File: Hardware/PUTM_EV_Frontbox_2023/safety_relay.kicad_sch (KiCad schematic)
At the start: 2 parts, among them Q1 2N7002

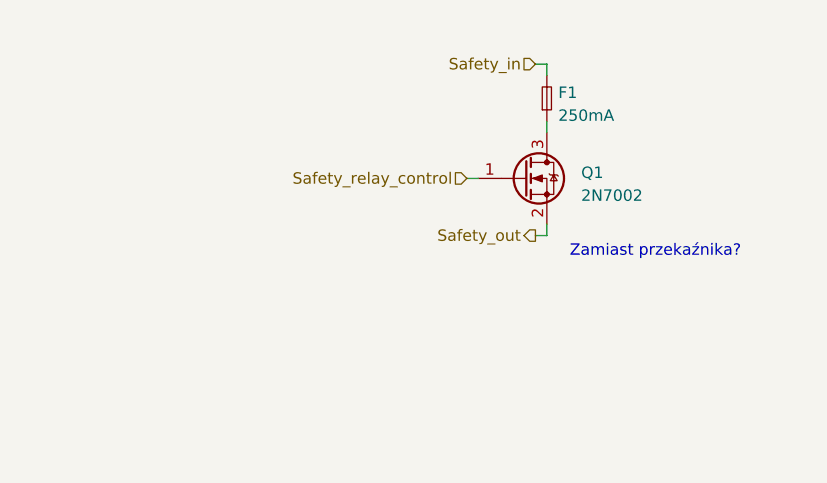
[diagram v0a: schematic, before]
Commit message: Added power section, replaced SWPS
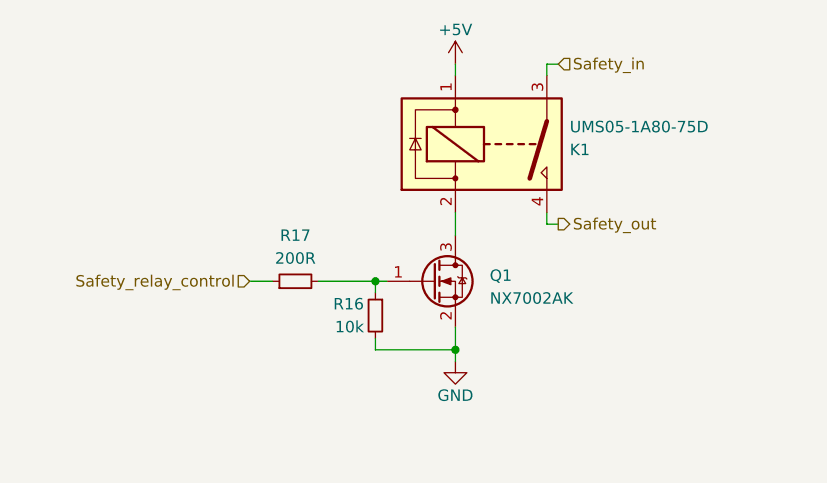
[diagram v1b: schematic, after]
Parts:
- removed F1: 250mA, symbol Device:Fuse_Small
- added K1: UMS05-1A80-75D, Relay_THT:Relay_StandexMeder_UMS, symbol Relay:UMS05-1A80-75D
- added R16: 10k, symbol Device:R_Small
- added R17: 200R, symbol Device:R_Small
- Q1: value 2N7002 -> NX7002AK
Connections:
- net Safety_in: now also K1.3
- net Safety_out: now also K1.4; no longer Q1.2 (S)
- net Safety_relay_control: now also R17.1; no longer Q1.1 (G)
- net at Q1.3 (D): now also K1.2
- new net: Q1.1 (G), R16.1, R17.2
- new net +5V: K1.1
- new net GND: Q1.2 (S), R16.2
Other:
- note removed: "Zamiast przekaźnika?"
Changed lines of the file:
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@@
     (comment 1 "Reviewer:")
   )
-  (wire (pts (xy 147.32 85.09) (xy 147.32 83.82))
-    (stroke (width 0) (type default))
-  )
-  (wire (pts (xy 138.43 78.74) (xy 139.7 78.74))
-    (stroke (width 0) (type default))
-  )
-  (wire (pts (xy 147.32 72.39) (xy 147.32 73.66))
-    (stroke (width 0) (type default))
-  )
-  (wire (pts (xy 146.05 85.09) (xy 147.32 85.09))
-    (stroke (width 0) (type default))
-  )
-  (wire (pts (xy 146.05 66.04) (xy 147.32 66.04))
-    (stroke (width 0) (type default))
-  )
-  (wire (pts (xy 147.32 66.04) (xy 147.32 67.31))
-    (stroke (width 0) (type default))
-  )
-  (text "Zamiast przekaźnika?" (at 149.86 87.63 0)
-    (effects (font (size 1.27 1.27)) (justify left bottom))
-  )
-  (hierarchical_label "Safety_out" (shape output) (at 146.05 85.09 180) (fields_autoplaced)
+  (junction (at 137.16 97.79) (diameter 0) (color 0 0 0 0)
+  )
+  (junction (at 128.27 90.17) (diameter 0) (color 0 0 0 0)
+  )
+  (wire (pts (xy 137.16 82.55) (xy 137.16 85.09))
+    (stroke (width 0) (type default))
+  )
+  (wire (pts (xy 128.27 97.79) (xy 137.16 97.79))
+    (stroke (width 0) (type default))
+  )
+  (wire (pts (xy 128.27 91.44) (xy 128.27 90.17))
+    (stroke (width 0) (type default))
+  )
+  (wire (pts (xy 121.92 90.17) (xy 128.27 90.17))
+    (stroke (width 0) (type default))
+  )
+  (wire (pts (xy 128.27 96.52) (xy 128.27 97.79))
+    (stroke (width 0) (type default))
+  )
+  (wire (pts (xy 137.16 95.25) (xy 137.16 97.79))
+    (stroke (width 0) (type default))
+  )
+  (wire (pts (xy 147.32 66.04) (xy 148.59 66.04))
+    (stroke (width 0) (type default))
+  )
+  (wire (pts (xy 137.16 97.79) (xy 137.16 99.06))
+    (stroke (width 0) (type default))
+  )
+  (wire (pts (xy 148.59 83.82) (xy 147.32 83.82))
+    (stroke (width 0) (type default))
+  )
+  (wire (pts (xy 147.32 67.31) (xy 147.32 66.04))
+    (stroke (width 0) (type default))
+  )
+  (wire (pts (xy 137.16 66.04) (xy 137.16 67.31))
+    (stroke (width 0) (type default))
+  )
+  (wire (pts (xy 114.3 90.17) (xy 116.84 90.17))
+    (stroke (width 0) (type default))
+  )
+  (wire (pts (xy 147.32 83.82) (xy 147.32 82.55))
+    (stroke (width 0) (type default))
+  )
+  (wire (pts (xy 128.27 90.17) (xy 129.54 90.17))
+    (stroke (width 0) (type default))
+  )
+  (hierarchical_label "Safety_out" (shape output) (at 148.59 83.82 0) (fields_autoplaced)
+    (effects (font (size 1.27 1.27)) (justify left))
+  )
+  (hierarchical_label "Safety_relay_control" (shape input) (at 114.3 90.17 180) (fields_autoplaced)
     (effects (font (size 1.27 1.27)) (justify right))
   )
-  (hierarchical_label "Safety_relay_control" (shape input) (at 138.43 78.74 180) (fields_autoplaced)
-    (effects (font (size 1.27 1.27)) (justify right))
-  )
-  (hierarchical_label "Safety_in" (shape input) (at 146.05 66.04 180) (fields_autoplaced)
-    (effects (font (size 1.27 1.27)) (justify right))
-  )
-  (symbol (lib_id "Transistor_FET:2N7002") (at 144.78 78.74 0) (unit 1)
+  (hierarchical_label "Safety_in" (shape input) (at 148.59 66.04 0) (fields_autoplaced)
+    (effects (font (size 1.27 1.27)) (justify left))
+  )
+  (symbol (lib_id "Device:R_Small") (at 128.27 93.98 0) (mirror y) (unit 1)
+    (in_bom yes) (on_board yes) (dnp no)
+    (property "Reference" "R16" (at 127 92.71 0)
+      (effects (font (size 1.27 1.27)) (justify left))
+    )
+    (property "Value" "10k" (at 127 95.25 0)
+      (effects (font (size 1.27 1.27)) (justify left))
+    )
+    (property "Footprint" "" (at 128.27 93.98 0)
+      (effects (font (size 1.27 1.27)) hide)
+    )
+    (property "Datasheet" "~" (at 128.27 93.98 0)
+      (effects (font (size 1.27 1.27)) hide)
+    )
+    (pin "1")
+    (pin "2")
+    (instances
+      (project "PUTM_EV_Frontbox_2023"
+        (path "/b652b05a-4e3d-4ad1-b032-18886abe7d45/9e051ed0-2f62-46c8-8b75-4aecd35a5af4"
+          (reference "R16") (unit 1)
+        )
+      )
+    )
+  )
+  (symbol (lib_id "Relay:UMS05-1A80-75D") (at 142.24 74.93 0) (mirror x) (unit 1)
+    (in_bom yes) (on_board yes) (dnp no)
+    (property "Reference" "K1" (at 149.86 75.565 0)
+      (effects (font (size 1.27 1.27)) (justify left))
+    )
+    (property "Value" "UMS05-1A80-75D" (at 149.86 73.025 0)
+      (effects (font (size 1.27 1.27)) (justify left))
+    )
+    (property "Footprint" "Relay_THT:Relay_StandexMeder_UMS" (at 149.86 73.66 0)
+      (effects (font (size 1.27 1.27)) (justify left) hide)
+    )
+    (property "Datasheet" "https://www.mouser.pl/ProductDetail/MEDER-electronic-Standex/UMS05-1A80-75D?qs=g9WlUi2XTnY%252B3JYCM9U0HQ%3D%3D" (at 142.24 74.93 0)
+      (effects (font (size 1.27 1.27)) hide)
+    )
+    (pin "1")
+    (pin "2")
+    (pin "3")
+    (pin "4")
+    (instances
+      (project "PUTM_EV_Frontbox_2023"
+        (path "/b652b05a-4e3d-4ad1-b032-18886abe7d45/9e051ed0-2f62-46c8-8b75-4aecd35a5af4"
+          (reference "K1") (unit 1)
+        )
+      )
+    )
+  )
+  (symbol (lib_id "Transistor_FET:2N7002") (at 134.62 90.17 0) (unit 1)
     (in_bom yes) (on_board yes) (dnp no) (fields_autoplaced)
-    (property "Reference" "Q1" (at 151.13 78.105 0)
-      (effects (font (size 1.27 1.27)) (justify left))
-    )
-    (property "Value" "2N7002" (at 151.13 80.645 0)
-      (effects (font (size 1.27 1.27)) (justify left))
-    )
-    (property "Footprint" "Package_TO_SOT_SMD:SOT-23" (at 149.86 80.645 0)
+    (property "Reference" "Q1" (at 140.97 89.535 0)
+      (effects (font (size 1.27 1.27)) (justify left))
+    )
+    (property "Value" "NX7002AK" (at 140.97 92.075 0)
+      (effects (font (size 1.27 1.27)) (justify left))
+    )
+    (property "Footprint" "Package_TO_SOT_SMD:SOT-23" (at 139.7 92.075 0)
       (effects (font (size 1.27 1.27) italic) (justify left) hide)
     )
-    (property "Datasheet" "https://www.mouser.pl/datasheet/2/916/2N7002NXAK-1623722.pdf" (at 144.78 78.74 0)
+    (property "Datasheet" "https://www.mouser.pl/datasheet/2/916/NX7002AK-1360313.pdf" (at 134.62 90.17 0)
       (effects (font (size 1.27 1.27)) (justify left) hide)
     )
@@
     )
   )
-  (symbol (lib_id "Device:Fuse_Small") (at 147.32 69.85 90) (unit 1)
+  (symbol (lib_id "power:+5V") (at 137.16 66.04 0) (unit 1)
     (in_bom yes) (on_board yes) (dnp no) (fields_autoplaced)
-    (property "Reference" "F1" (at 148.59 69.215 90)
-      (effects (font (size 1.27 1.27)) (justify right))
-    )
-    (property "Value" "250mA" (at 148.59 71.755 90)
-      (effects (font (size 1.27 1.27)) (justify right))
-    )
-    (property "Footprint" "" (at 147.32 69.85 0)
-      (effects (font (size 1.27 1.27)) hide)
-    )
-    (property "Datasheet" "~" (at 147.32 69.85 0)
-      (effects (font (size 1.27 1.27)) hide)
-    )
-    (pin "1")
-    (pin "2")
-    (instances
-      (project "PUTM_EV_Frontbox_2023"
-        (path "/b652b05a-4e3d-4ad1-b032-18886abe7d45/9e051ed0-2f62-46c8-8b75-4aecd35a5af4"
-          (reference "F1") (unit 1)
-        )
-      )
+    (property "Reference" "#PWR075" (at 137.16 69.85 0)
+      (effects (font (size 1.27 1.27)) hide)
+    )
+    (property "Value" "+5V" (at 137.16 62.23 0)
+      (effects (font (size 1.27 1.27)))
+    )
+    (property "Footprint" "" (at 137.16 66.04 0)
+      (effects (font (size 1.27 1.27)) hide)
+    )
+    (property "Datasheet" "" (at 137.16 66.04 0)
+      (effects (font (size 1.27 1.27)) hide)
+    )
+    (pin "1")
+    (instances
+      (project "PUTM_EV_Frontbox_2023"
+        (path "/b652b05a-4e3d-4ad1-b032-18886abe7d45/9e051ed0-2f62-46c8-8b75-4aecd35a5af4"
+          (reference "#PWR075") (unit 1)
+        )
+      )
+    )
+  )
+  (symbol (lib_id "power:GND") (at 137.16 99.06 0) (unit 1)
+    (in_bom yes) (on_board yes) (dnp no)
+    (property "Reference" "#PWR074" (at 137.16 105.41 0)
+      (effects (font (size 1.27 1.27)) hide)
+    )
+    (property "Value" "GND" (at 137.16 102.87 0)
+      (effects (font (size 1.27 1.27)))
+    )
+    (property "Footprint" "" (at 137.16 99.06 0)
+      (effects (font (size 1.27 1.27)) hide)
+    )
+    (property "Datasheet" "" (at 137.16 99.06 0)
+      (effects (font (size 1.27 1.27)) hide)
+    )
+    (pin "1")
+    (instances
+      (project "PUTM_EV_Frontbox_2023"
+        (path "/b652b05a-4e3d-4ad1-b032-18886abe7d45/9e051ed0-2f62-46c8-8b75-4aecd35a5af4"
+          (reference "#PWR074") (unit 1)
+        )
+      )
+    )
+  )
+  (symbol (lib_id "Device:R_Small") (at 119.38 90.17 90) (unit 1)
+    (in_bom yes) (on_board yes) (dnp no) (fields_autoplaced)
+    (property "Reference" "R17" (at 119.38 85.09 90)
+      (effects (font (size 1.27 1.27)))
+    )
+    (property "Value" "200R" (at 119.38 87.63 90)
+      (effects (font (size 1.27 1.27)))
+    )
+    (property "Footprint" "" (at 119.38 90.17 0)
+      (effects (font (size 1.27 1.27)) hide)
+    )
+    (property "Datasheet" "~" (at 119.38 90.17 0)
+      (effects (font (size 1.27 1.27)) hide)
+    )
+    (pin "1")
+    (pin "2")
+    (instances
+      (project "PUTM_EV_Frontbox_2023"
+        (path "/b652b05a-4e3d-4ad1-b032-18886abe7d45/9e051ed0-2f62-46c8-8b75-4aecd35a5af4"
+          (reference "R17") (unit 1)
+        )
+      )

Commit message: Added MCU wiring
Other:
- title: Safety relay -> Safety relay control
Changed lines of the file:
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@@
   (paper "A4")
   (title_block
-    (title "Safety relay")
+    (title "Safety relay control")
     (date "2023-02-24")
     (rev "${REVISION}")

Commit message: Schematic ready for review
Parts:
- renumbered R16 to R10, R17 to R9
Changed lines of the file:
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@@
   (title_block
     (title "Safety relay control")
-    (date "2023-02-24")
+    (date "2023-03-11")
     (rev "${REVISION}")
     (company "Author: Szymon Kostrubiec")
@@
   (symbol (lib_id "Device:R_Small") (at 128.27 93.98 0) (mirror y) (unit 1)
     (in_bom yes) (on_board yes) (dnp no)
-    (property "Reference" "R16" (at 127 92.71 0)
+    (property "Reference" "R10" (at 127 92.71 0)
       (effects (font (size 1.27 1.27)) (justify left))
     )
@@
       (project "PUTM_EV_Frontbox_2023"
         (path "/b652b05a-4e3d-4ad1-b032-18886abe7d45/9e051ed0-2f62-46c8-8b75-4aecd35a5af4"
-          (reference "R16") (unit 1)
+          (reference "R10") (unit 1)
         )
       )
@@
   (symbol (lib_id "power:+5V") (at 137.16 66.04 0) (unit 1)
     (in_bom yes) (on_board yes) (dnp no) (fields_autoplaced)
-    (property "Reference" "#PWR075" (at 137.16 69.85 0)
+    (property "Reference" "#PWR070" (at 137.16 69.85 0)
       (effects (font (size 1.27 1.27)) hide)
     )
@@
       (project "PUTM_EV_Frontbox_2023"
         (path "/b652b05a-4e3d-4ad1-b032-18886abe7d45/9e051ed0-2f62-46c8-8b75-4aecd35a5af4"
-          (reference "#PWR075") (unit 1)
+          (reference "#PWR070") (unit 1)
         )
       )
@@
   (symbol (lib_id "power:GND") (at 137.16 99.06 0) (unit 1)
     (in_bom yes) (on_board yes) (dnp no)
-    (property "Reference" "#PWR074" (at 137.16 105.41 0)
+    (property "Reference" "#PWR071" (at 137.16 105.41 0)
       (effects (font (size 1.27 1.27)) hide)
     )
@@
       (project "PUTM_EV_Frontbox_2023"
         (path "/b652b05a-4e3d-4ad1-b032-18886abe7d45/9e051ed0-2f62-46c8-8b75-4aecd35a5af4"
-          (reference "#PWR074") (unit 1)
+          (reference "#PWR071") (unit 1)
         )
       )
@@
   (symbol (lib_id "Device:R_Small") (at 119.38 90.17 90) (unit 1)
     (in_bom yes) (on_board yes) (dnp no) (fields_autoplaced)
-    (property "Reference" "R17" (at 119.38 85.09 90)
+    (property "Reference" "R9" (at 119.38 85.09 90)
       (effects (font (size 1.27 1.27)))
     )
@@
       (project "PUTM_EV_Frontbox_2023"
         (path "/b652b05a-4e3d-4ad1-b032-18886abe7d45/9e051ed0-2f62-46c8-8b75-4aecd35a5af4"
-          (reference "R17") (unit 1)
-        )
-      )
+          (reference "R9") (unit 1)
+        )
+      )

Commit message: Schematic modified, footprints assigned
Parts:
- R10, R9: footprint (none) -> Resistor_SMD:R_0402_1005Metric
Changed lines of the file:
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@@
       (effects (font (size 1.27 1.27)) (justify left))
     )
-    (property "Footprint" "" (at 128.27 93.98 0)
+    (property "Footprint" "Resistor_SMD:R_0402_1005Metric" (at 128.27 93.98 0)
       (effects (font (size 1.27 1.27)) hide)
     )
@@
       (effects (font (size 1.27 1.27)))
     )
-    (property "Footprint" "" (at 119.38 90.17 0)
+    (property "Footprint" "Resistor_SMD:R_0402_1005Metric" (at 119.38 90.17 0)
       (effects (font (size 1.27 1.27)) hide)
     )

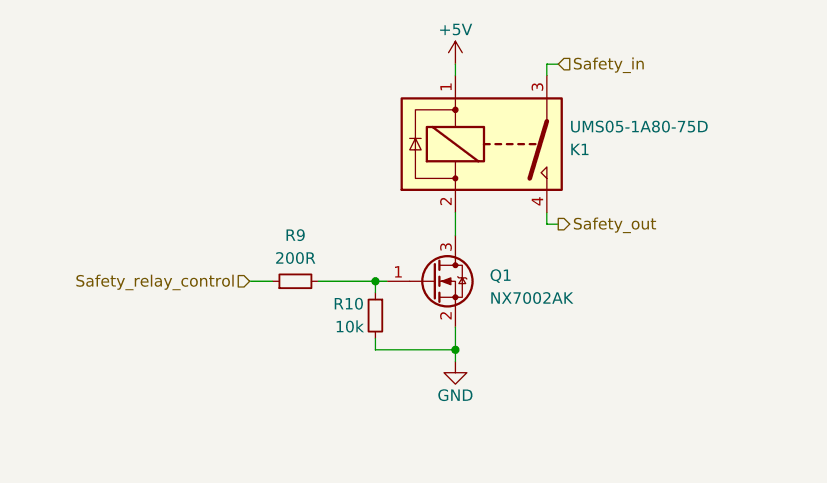
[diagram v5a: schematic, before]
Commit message: Changed board outline and layout to match ASB
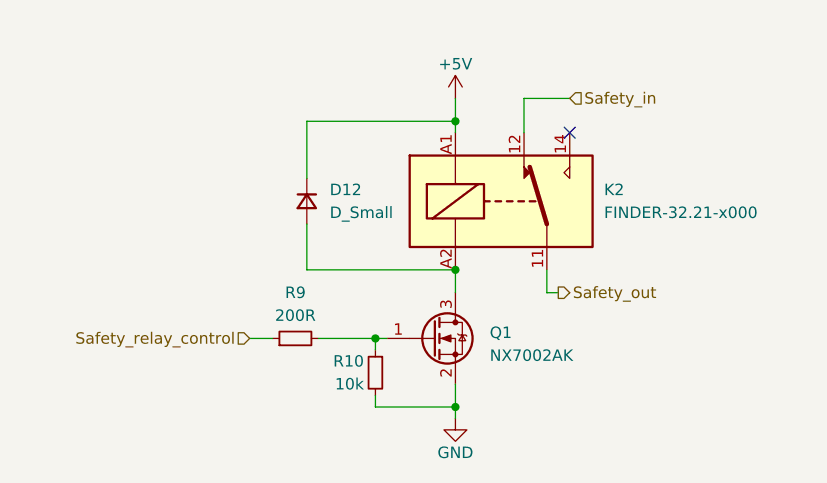
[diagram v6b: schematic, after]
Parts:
- removed K1: UMS05-1A80-75D, Relay_THT:Relay_StandexMeder_UMS, symbol Relay:UMS05-1A80-75D
- added D12: D_Small, Diode_SMD:D_0805_2012Metric_Pad1.15x1.40mm_HandSolder, symbol Device:D_Small
- added K2: FINDER-32.21-x000, Relay_THT:Relay_SPDT_Finder_32.21-x000, symbol Relay:FINDER-32.21-x000
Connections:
- net +5V: now also D12.1 (K), K2.A1
- net Safety_in: now also K2.12
- net Safety_out: now also K2.11
- net at Q1.3 (D): now also D12.2 (A), K2.A2
- no-connect marks 0 -> 1
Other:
- moved on the sheet: Q1, R10, R9

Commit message: Added gearbox temperature sensors on schematic
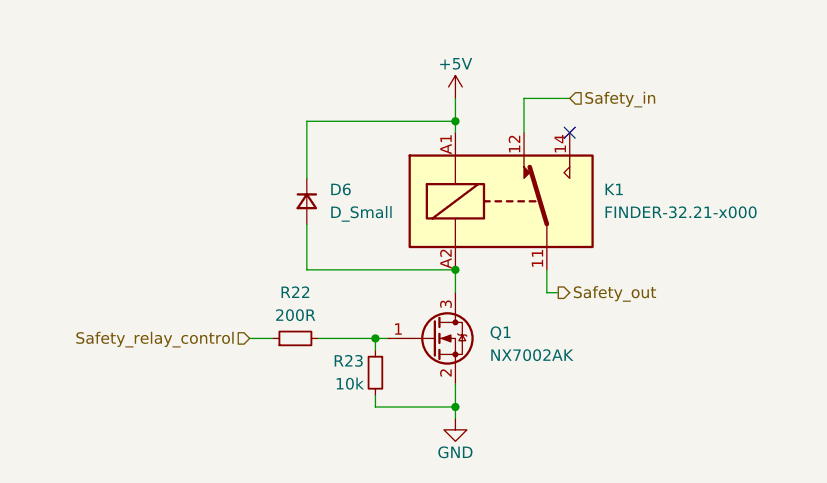
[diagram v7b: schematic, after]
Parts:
- renumbered D12 to D6, K2 to K1, R9 to R22, R10 to R23
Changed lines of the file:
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@@
   (symbol (lib_id "Device:R_Small") (at 128.27 100.33 0) (mirror y) (unit 1)
     (in_bom yes) (on_board yes) (dnp no)
-    (property "Reference" "R10" (at 127 99.06 0)
+    (property "Reference" "R23" (at 127 99.06 0)
       (effects (font (size 1.27 1.27)) (justify left))
     )
@@
       (project "PUTM_EV_Frontbox_2023"
         (path "/b652b05a-4e3d-4ad1-b032-18886abe7d45/9e051ed0-2f62-46c8-8b75-4aecd35a5af4"
-          (reference "R10") (unit 1)
+          (reference "R23") (unit 1)
         )
       )
@@
   (symbol (lib_id "Relay:FINDER-32.21-x000") (at 142.24 81.28 0) (unit 1)
     (in_bom yes) (on_board yes) (dnp no) (fields_autoplaced)
-    (property "Reference" "K2" (at 153.67 80.01 0)
+    (property "Reference" "K1" (at 153.67 80.01 0)
       (effects (font (size 1.27 1.27)) (justify left))
     )
@@
     (instances
       (project "PUTM_EV_Frontbox_2023"
-        (path "/b652b05a-4e3d-4ad1-b032-18886abe7d45"
-          (reference "K2") (unit 1)
-        )
         (path "/b652b05a-4e3d-4ad1-b032-18886abe7d45/9e051ed0-2f62-46c8-8b75-4aecd35a5af4"
-          (reference "K2") (unit 1)
+          (reference "K1") (unit 1)
         )
       )
@@
   (symbol (lib_id "Device:D_Small") (at 120.65 81.28 270) (unit 1)
     (in_bom yes) (on_board yes) (dnp no) (fields_autoplaced)
-    (property "Reference" "D12" (at 123.19 80.01 90)
+    (property "Reference" "D6" (at 123.19 80.01 90)
       (effects (font (size 1.27 1.27)) (justify left))
     )
@@
       (project "PUTM_EV_Frontbox_2023"
         (path "/b652b05a-4e3d-4ad1-b032-18886abe7d45/9e051ed0-2f62-46c8-8b75-4aecd35a5af4"
-          (reference "D12") (unit 1)
+          (reference "D6") (unit 1)
         )
       )
@@
   (symbol (lib_id "power:+5V") (at 137.16 69.85 0) (unit 1)
     (in_bom yes) (on_board yes) (dnp no) (fields_autoplaced)
-    (property "Reference" "#PWR070" (at 137.16 73.66 0)
+    (property "Reference" "#PWR079" (at 137.16 73.66 0)
       (effects (font (size 1.27 1.27)) hide)
     )
@@
       (project "PUTM_EV_Frontbox_2023"
         (path "/b652b05a-4e3d-4ad1-b032-18886abe7d45/9e051ed0-2f62-46c8-8b75-4aecd35a5af4"
-          (reference "#PWR070") (unit 1)
+          (reference "#PWR079") (unit 1)
         )
       )
@@
   (symbol (lib_id "power:GND") (at 137.16 105.41 0) (unit 1)
     (in_bom yes) (on_board yes) (dnp no)
-    (property "Reference" "#PWR071" (at 137.16 111.76 0)
+    (property "Reference" "#PWR080" (at 137.16 111.76 0)
       (effects (font (size 1.27 1.27)) hide)
     )
@@
       (project "PUTM_EV_Frontbox_2023"
         (path "/b652b05a-4e3d-4ad1-b032-18886abe7d45/9e051ed0-2f62-46c8-8b75-4aecd35a5af4"
-          (reference "#PWR071") (unit 1)
+          (reference "#PWR080") (unit 1)
         )
       )
@@
   (symbol (lib_id "Device:R_Small") (at 119.38 96.52 90) (unit 1)
     (in_bom yes) (on_board yes) (dnp no) (fields_autoplaced)
-    (property "Reference" "R9" (at 119.38 91.44 90)
+    (property "Reference" "R22" (at 119.38 91.44 90)
       (effects (font (size 1.27 1.27)))
     )
@@
       (project "PUTM_EV_Frontbox_2023"
         (path "/b652b05a-4e3d-4ad1-b032-18886abe7d45/9e051ed0-2f62-46c8-8b75-4aecd35a5af4"
-          (reference "R9") (unit 1)
+          (reference "R22") (unit 1)
         )
       )
